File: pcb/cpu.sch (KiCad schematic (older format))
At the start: 7 parts, among them J1 Conn_01x16, J2 Conn_01x16, U1 74HC86, U2 74AHC1G08, U3 74HC86, U4 74AHC1G08, U5 74AHC1G32

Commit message: wip schematics
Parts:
- removed J1: Conn_01x16, symbol Connector_Generic:Conn_01x16
- removed U2: 74AHC1G08, symbol 74xGxx:74AHC1G08
- removed U5: 74AHC1G32, symbol 74xGxx:74AHC1G32
- added J1: Conn_01x32_Male, symbol Connector:Conn_01x32_Male
- added U10, U11, U6, U7, U8, U9: 74AHC1G08, symbol 74xGxx:74AHC1G08
- added U12, U13, U14, U2, U5: 74HC86, symbol 74xx:74HC86
- added U15, U16, U17: 74AHC1G32, symbol 74xGxx:74AHC1G32
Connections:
- wire segments 28 -> 90

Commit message: labels
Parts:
- removed J1: Conn_01x32_Male, symbol Connector:Conn_01x32_Male
- removed J2: Conn_01x16, symbol Connector_Generic:Conn_01x16
- removed U1: 74HC86, symbol 74xx:74HC86
- removed U7: 74AHC1G08, symbol 74xGxx:74AHC1G08
- added U?: 74AHC1G08, symbol 74xGxx:74AHC1G08
- added U?: 74HC86, symbol 74xx:74HC86
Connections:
- net labels added: a0, a1, a2, a3, b0, b1, b2, b3, sum0, sum1, sum2, sum3
- wire segments 90 -> 74
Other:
- moved on the sheet: U10, U11, U12A, U13A, U14A, U15, U16, U17, U2A, U3A, U4, U5A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

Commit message: 16bit adder
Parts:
- added U1, U21, U23, U24, U25, U26, U35, U36, U37, U38, U43, U44, U45, U46, U55, U56, U57, U58, U63, U64, U65, U72, U73, U74: 74HC86, symbol 74xx:74HC86
- added U19, U20, U27, U28, U29, U30, U31, U32, U33, U34, U47, U48, U49, U50, U51, U52, U53, U54, U66, U67, U68, U69, U70, U71: 74AHC1G08, symbol 74xGxx:74AHC1G08
- added U22, U39, U40, U41, U42, U59, U60, U61, U62, U75, U76, U77: 74AHC1G32, symbol 74xGxx:74AHC1G32
- gave numbers to parts that had none: 2
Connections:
- net GND: now also U19.3 (GND), U20.3 (GND), U22.3 (GND), U27.3 (GND), U28.3 (GND), U29.3 (GND), U30.3 (GND), U31.3 (GND), U32.3 (GND), U33.3 (GND), U34.3 (GND), U39.3 (GND), U40.3 (GND), U41.3 (GND), U42.3 (GND), U47.3 (GND), U48.3 (GND), U49.3 (GND), U50.3 (GND), U51.3 (GND), U52.3 (GND), U53.3 (GND), U54.3 (GND), U59.3 (GND), U60.3 (GND), U61.3 (GND), U62.3 (GND), U66.3 (GND), U67.3 (GND), U68.3 (GND), U69.3 (GND), U70.3 (GND), U71.3 (GND), U75.3 (GND), U76.3 (GND), U77.3 (GND)
- net VCC: now also U19.5 (VCC), U20.5 (VCC), U22.5 (VCC), U27.5 (VCC), U28.5 (VCC), U29.5 (VCC), U30.5 (VCC), U31.5 (VCC), U32.5 (VCC), U33.5 (VCC), U34.5 (VCC), U39.5 (VCC), U40.5 (VCC), U41.5 (VCC), U42.5 (VCC), U47.5 (VCC), U48.5 (VCC), U49.5 (VCC), U50.5 (VCC), U51.5 (VCC), U52.5 (VCC), U53.5 (VCC), U54.5 (VCC), U59.5 (VCC), U60.5 (VCC), U61.5 (VCC), U62.5 (VCC), U66.5 (VCC), U67.5 (VCC), U68.5 (VCC), U69.5 (VCC), U70.5 (VCC), U71.5 (VCC), U75.5 (VCC), U76.5 (VCC), U77.5 (VCC)
- net at U16.4: now also U19.1, U21.1
- new net: U19.4, U22.1
- new net: U20.4, U22.2
- new net: U22.4, U27.1, U35.1
- new net: U1.3, U19.2, U21.2
- new net: U27.4, U39.1
- new net: U28.4, U39.2
- new net: U29.1, U36.1, U39.4
- new net: U23.3, U27.2, U35.2
- new net: U29.4, U40.1
- new net: U30.4, U40.2
- new net: U31.1, U37.1, U40.4
- new net: U24.3, U29.2, U36.2
- new net: U31.4, U41.1
- new net: U32.4, U41.2
- new net: U33.1, U38.1, U41.4
- new net: U25.3, U31.2, U37.2
- new net: U33.4, U42.1
- new net: U34.4, U42.2
- new net: U42.4, U47.1, U55.1
- new net: U26.3, U33.2, U38.2
- new net: U47.4, U59.1
- new net: U48.4, U59.2
- new net: U49.1, U56.1, U59.4
- new net: U43.3, U47.2, U55.2
- new net: U49.4, U60.1
- new net: U50.4, U60.2
- new net: U51.1, U57.1, U60.4
- new net: U44.3, U49.2, U56.2
- new net: U51.4, U61.1
- new net: U52.4, U61.2
- new net: U53.1, U58.1, U61.4
- new net: U45.3, U51.2, U57.2
- new net: U53.4, U62.1
- new net: U54.4, U62.2
- new net: U62.4, U66.1, U72.1
- new net: U46.3, U53.2, U58.2
- new net: U66.4, U75.1
- new net: U67.4, U75.2
- new net: U68.1, U73.1, U75.4
- new net: U63.3, U66.2, U72.2
- new net: U68.4, U76.1
- new net: U69.4, U76.2
- new net: U70.1, U74.1, U76.4
- new net: U64.3, U68.2, U73.2
- new net: U70.4, U77.1
- new net: U71.4, U77.2
- new net: U65.3, U70.2, U74.2
- new net a10: U44.1, U50.1
- new net a11: U45.1, U52.1
- new net a12: U46.1, U54.1
- new net a13: U63.1, U67.1
- new net a14: U64.1, U69.1
- new net a15: U65.1, U71.1
- new net a4: U1.1, U20.1
- new net a5: U23.1, U28.1
- new net a6: U24.1, U30.1
- new net a7: U25.1, U32.1
- new net a8: U26.1, U34.1
- new net a9: U43.1, U48.1
- new net b10: U44.2, U50.2
- new net b11: U45.2, U52.2
- new net b12: U46.2, U54.2
- new net b13: U63.2, U67.2
- new net b14: U64.2, U69.2
- new net b15: U65.2, U71.2
- new net b4: U1.2, U20.2
- new net b5: U23.2, U28.2
- new net b6: U24.2, U30.2
- new net b7: U25.2, U32.2
- new net b8: U26.2, U34.2
- new net b9: U43.2, U48.2
- new net c: U77.4
- new net sum10: U56.3
- new net sum11: U57.3
- new net sum12: U58.3
- new net sum13: U72.3
- new net sum14: U73.3
- new net sum15: U74.3
- new net sum4: U21.3
- new net sum5: U35.3
- new net sum6: U36.3
- new net sum7: U37.3
- new net sum8: U38.3
- new net sum9: U55.3
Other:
- moved on the sheet: U10, U11, U12A, U13A, U14A, U15, U16, U17, U18, U2A, U3A, U4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

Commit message: adder 16 bit netlist and footprints
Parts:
- U1, U10, U11, U12, U13, U14, U15, U16, U17, U18, U19, U2, U20, U21, U22, U23, U24, U25, U26, U27, U28, U29, U3, U30, U31, U32, U33, U34, U35, U36, U37, U38, U39, U4, U40, U41, U42, U43, U44, U45, U46, U47, U48, U49, U5, U50, U51, U52, U53, U54, U55, U56, U57, U58, U59, U6, U60, U61, U62, U63, U64, U65, U66, U67, U68, U69, U7, U70, U71, U72, U73, U74, U75, U76, U77, U8, U9: footprint (none) -> Package_SO:SOIC-14_3.9x8.7mm_P1.27mm

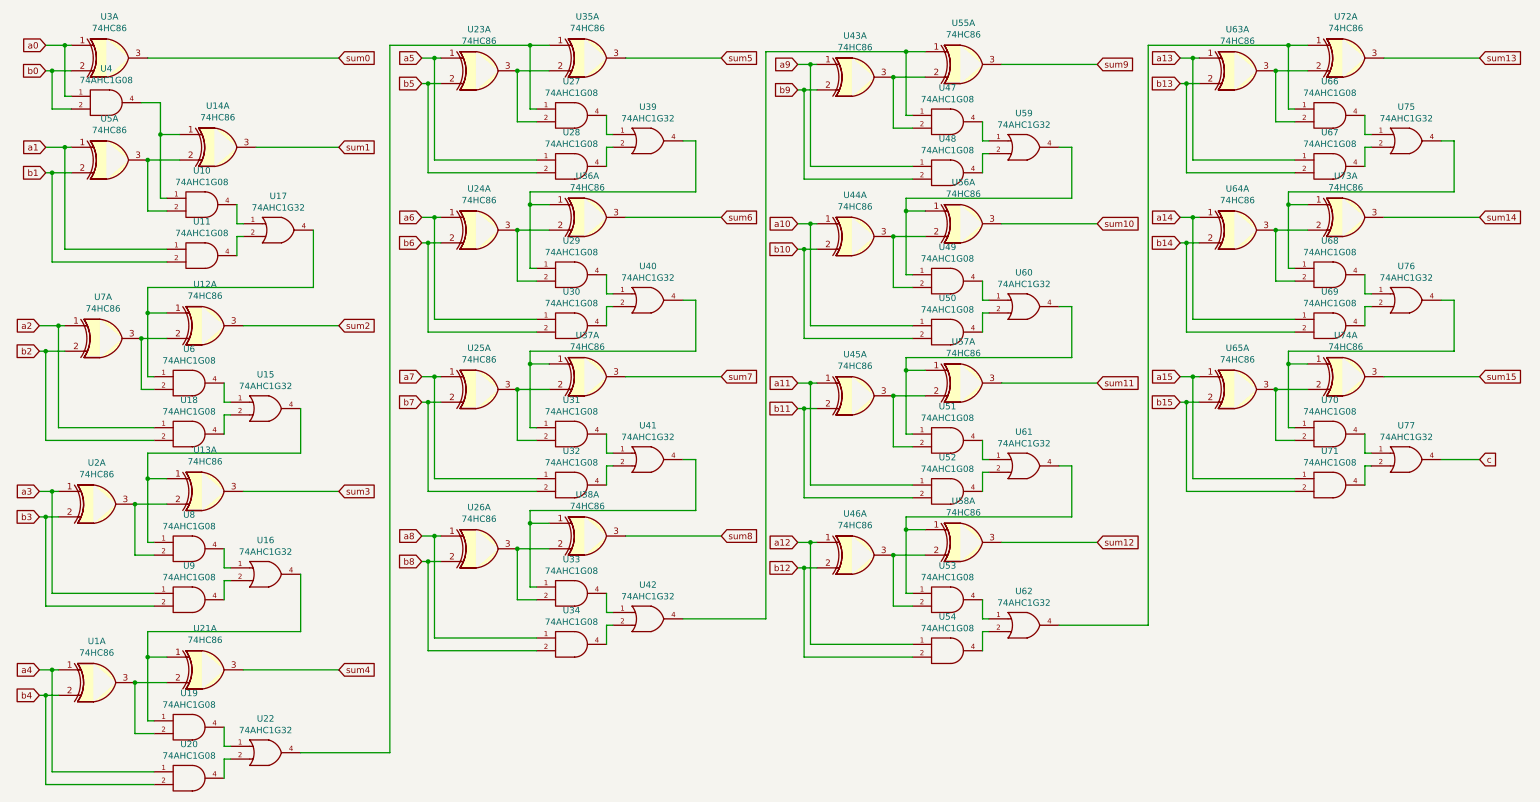
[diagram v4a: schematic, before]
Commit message: 16 bit adder from 74LS283
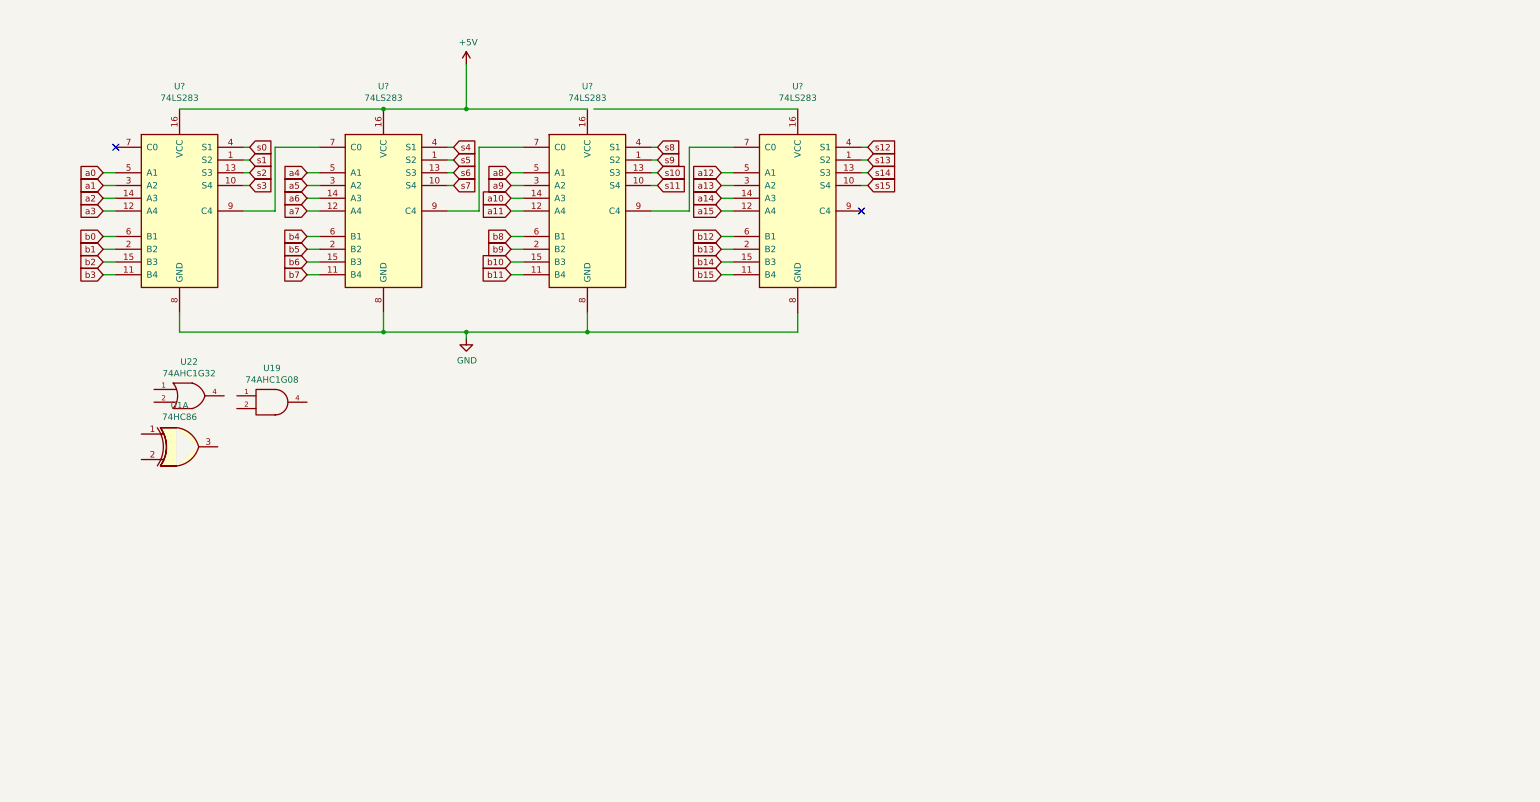
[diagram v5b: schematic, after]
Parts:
- removed U10, U11, U18, U20, U27, U28, U29, U30, U31, U32, U33, U34, U4, U47, U48, U49, U50, U51, U52, U53, U54, U6, U66, U67, U68, U69, U70, U71, U8, U9: 74AHC1G08, Package_SO:SOIC-14_3.9x8.7mm_P1.27mm, symbol 74xGxx:74AHC1G08
- removed U12, U13, U14, U2, U21, U23, U24, U25, U26, U3, U35, U36, U37, U38, U43, U44, U45, U46, U5, U55, U56, U57, U58, U63, U64, U65, U7, U72, U73, U74: 74HC86, Package_SO:SOIC-14_3.9x8.7mm_P1.27mm, symbol 74xx:74HC86
- removed U15, U16, U17, U39, U40, U41, U42, U59, U60, U61, U62, U75, U76, U77: 74AHC1G32, Package_SO:SOIC-14_3.9x8.7mm_P1.27mm, symbol 74xGxx:74AHC1G32
- added U? (x4): 74LS283, symbol 74xx:74LS283
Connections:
- net GND: now also U?.8 (GND), U?.8 (GND), U?.8 (GND), U?.8 (GND)
- net a0: now also U?.5 (A1)
- net a1: now also U?.3 (A2)
- net a10: now also U?.14 (A3)
- net a11: now also U?.12 (A4)
- net a12: now also U?.5 (A1)
- net a13: now also U?.3 (A2)
- net a14: now also U?.14 (A3)
- net a15: now also U?.12 (A4)
- net a2: now also U?.14 (A3)
- net a3: now also U?.12 (A4)
- net a4: now also U?.5 (A1); no longer U1.1
- net a5: now also U?.3 (A2)
- net a6: now also U?.14 (A3)
- net a7: now also U?.12 (A4)
- net a8: now also U?.5 (A1)
- net a9: now also U?.3 (A2)
- net b0: now also U?.6 (B1)
- net b1: now also U?.2 (B2)
- net b10: now also U?.15 (B3)
- net b11: now also U?.11 (B4)
- net b12: now also U?.6 (B1)
- net b13: now also U?.2 (B2)
- net b14: now also U?.15 (B3)
- net b15: now also U?.11 (B4)
- net b2: now also U?.15 (B3)
- net b3: now also U?.11 (B4)
- net b4: now also U?.6 (B1); no longer U1.2
- net b5: now also U?.2 (B2)
- net b6: now also U?.15 (B3)
- net b7: now also U?.11 (B4)
- net b8: now also U?.6 (B1)
- net b9: now also U?.2 (B2)
- net at U22.1: no longer U19.4
- net at U19.2: no longer U1.3
- new net: U?.7 (C0), U?.9 (C4) (x3)
- new net +5V: U?.16 (VCC), U?.16 (VCC), U?.16 (VCC)
- new net s0: U?.4 (S1)
- new net s1: U?.1 (S2)
- new net s10: U?.13 (S3)
- new net s11: U?.10 (S4)
- new net s12: U?.4 (S1)
- new net s13: U?.1 (S2)
- new net s14: U?.13 (S3)
- new net s15: U?.10 (S4)
- new net s2: U?.13 (S3)
- new net s3: U?.10 (S4)
- new net s4: U?.4 (S1)
- new net s5: U?.1 (S2)
- new net s6: U?.13 (S3)
- new net s7: U?.10 (S4)
- new net s8: U?.4 (S1)
- new net s9: U?.1 (S2)
- no-connect marks 0 -> 2
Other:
- moved on the sheet: U19, U1A, U22

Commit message: wip
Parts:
- removed U1: 74HC86, Package_SO:SOIC-14_3.9x8.7mm_P1.27mm, symbol 74xx:74HC86
- removed U19: 74AHC1G08, Package_SO:SOIC-14_3.9x8.7mm_P1.27mm, symbol 74xGxx:74AHC1G08
- removed U22: 74AHC1G32, Package_SO:SOIC-14_3.9x8.7mm_P1.27mm, symbol 74xGxx:74AHC1G32
- added J1: Conn_02x16_Counter_Clockwise, Connector_PinHeader_1.27mm:PinHeader_2x16_P1.27mm_Vertical, symbol Connector_Generic:Conn_02x16_Counter_Clockwise
- added J2: Conn_01x16, Connector_PinHeader_1.27mm:PinHeader_1x16_P1.27mm_Vertical, symbol Connector_Generic:Conn_01x16
- added U? (x3): 74LS21, symbol 74xx:74LS21
- U1, U2, U3, U4: renamed from U?; footprint (none) -> Package_SO:SOIC-16_3.9x9.9mm_P1.27mm
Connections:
- net a0: now also J1.1 (Pin_1)
- net a1: now also J1.2 (Pin_2)
- net a10: now also J1.11 (Pin_11)
- net a11: now also J1.12 (Pin_12)
- net a12: now also J1.13 (Pin_13)
- net a13: now also J1.14 (Pin_14)
- net a14: now also J1.15 (Pin_15)
- net a15: now also J1.16 (Pin_16)
- net a2: now also J1.3 (Pin_3)
- net a3: now also J1.4 (Pin_4)
- net a4: now also J1.5 (Pin_5)
- net a5: now also J1.6 (Pin_6)
- net a6: now also J1.7 (Pin_7)
- net a7: now also J1.8 (Pin_8)
- net a8: now also J1.9 (Pin_9)
- net a9: now also J1.10 (Pin_10)
- net b0: now also J1.32 (Pin_32)
- net b1: now also J1.31 (Pin_31)
- net b10: now also J1.22 (Pin_22)
- net b11: now also J1.21 (Pin_21)
- net b12: now also J1.20 (Pin_20)
- net b13: now also J1.19 (Pin_19)
- net b14: now also J1.18 (Pin_18)
- net b15: now also J1.17 (Pin_17)
- net b2: now also J1.30 (Pin_30)
- net b3: now also J1.29 (Pin_29)
- net b4: now also J1.28 (Pin_28)
- net b5: now also J1.27 (Pin_27)
- net b6: now also J1.26 (Pin_26)
- net b7: now also J1.25 (Pin_25)
- net b8: now also J1.24 (Pin_24)
- net b9: now also J1.23 (Pin_23)
- net s0: now also J2.1 (Pin_1)
- net s1: now also J2.2 (Pin_2)
- net s10: now also J2.11 (Pin_11)
- net s11: now also J2.12 (Pin_12)
- net s12: now also J2.13 (Pin_13)
- net s13: now also J2.14 (Pin_14)
- net s14: now also J2.15 (Pin_15)
- net s15: now also J2.16 (Pin_16)
- net s2: now also J2.3 (Pin_3)
- net s3: now also J2.4 (Pin_4)
- net s4: now also J2.5 (Pin_5)
- net s5: now also J2.6 (Pin_6)
- net s6: now also J2.7 (Pin_7)
- net s7: now also J2.8 (Pin_8)
- net s8: now also J2.9 (Pin_9)
- net s9: now also J2.10 (Pin_10)
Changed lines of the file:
@@
 $EndDescr
 $Comp
-L 74xx:74LS283 U?
+L 74xx:74LS283 U1
 U 1 1 5CE54893
 P 1750 2100
-F 0 "U?" H 1750 3078 50  0000 C CNN
+F 0 "U1" H 1750 3078 50  0000 C CNN
 F 1 "74LS283" H 1750 2987 50  0000 C CNN
-F 2 "" H 1750 2100 50  0001 C CNN
+F 2 "Package_SO:SOIC-16_3.9x9.9mm_P1.27mm" H 1750 2100 50  0001 C CNN
 F 3 "http://www.ti.com/lit/gpn/sn74LS283" H 1750 2100 50  0001 C CNN
 	1    1750 2100
@@
 $EndComp
 $Comp
-L 74xx:74LS283 U?
+L 74xx:74LS283 U2
 U 1 1 5CE54F63
 P 3350 2100
-F 0 "U?" H 3350 3078 50  0000 C CNN
+F 0 "U2" H 3350 3078 50  0000 C CNN
 F 1 "74LS283" H 3350 2987 50  0000 C CNN
-F 2 "" H 3350 2100 50  0001 C CNN
+F 2 "Package_SO:SOIC-16_3.9x9.9mm_P1.27mm" H 3350 2100 50  0001 C CNN
 F 3 "http://www.ti.com/lit/gpn/sn74LS283" H 3350 2100 50  0001 C CNN
 	1    3350 2100
@@
 $EndComp
 $Comp
-L 74xx:74HC86 U1
-U 1 1 5CC11E00
-P 1750 3950
-F 0 "U1" H 1750 4275 50  0000 C CNN
-F 1 "74HC86" H 1750 4184 50  0000 C CNN
-F 2 "Package_SO:SOIC-14_3.9x8.7mm_P1.27mm" H 1750 3950 50  0001 C CNN
-F 3 "http://www.ti.com/lit/gpn/sn74HC86" H 1750 3950 50  0001 C CNN
-	1    1750 3950
-	1    0    0    -1
-$EndComp
-$Comp
-L 74xGxx:74AHC1G08 U19
-U 1 1 5CC11DE5
-P 2500 3600
-F 0 "U19" H 2475 3867 50  0000 C CNN
-F 1 "74AHC1G08" H 2475 3776 50  0000 C CNN
-F 2 "Package_SO:SOIC-14_3.9x8.7mm_P1.27mm" H 2500 3600 50  0001 C CNN
-F 3 "http://www.ti.com/lit/sg/scyt129e/scyt129e.pdf" H 2500 3600 50  0001 C CNN
-	1    2500 3600
-	1    0    0    -1
-$EndComp
-$Comp
-L 74xGxx:74AHC1G32 U22
-U 1 1 5CC11DD7
-P 1850 3550
-F 0 "U22" H 1825 3817 50  0000 C CNN
-F 1 "74AHC1G32" H 1825 3726 50  0000 C CNN
-F 2 "Package_SO:SOIC-14_3.9x8.7mm_P1.27mm" H 1850 3550 50  0001 C CNN
-F 3 "http://www.ti.com/lit/sg/scyt129e/scyt129e.pdf" H 1850 3550 50  0001 C CNN
-	1    1850 3550
-	1    0    0    -1
-$EndComp
-$Comp
-L power:+5V #PWR?
+L power:+5V #PWR0101
 U 1 1 5CE5585C
 P 4000 950
-F 0 "#PWR?" H 4000 800 50  0001 C CNN
+F 0 "#PWR0101" H 4000 800 50  0001 C CNN
 F 1 "+5V" H 4015 1123 50  0000 C CNN
 F 2 "" H 4000 950 50  0001 C CNN
@@
 $EndComp
 $Comp
-L 74xx:74LS283 U?
+L 74xx:74LS283 U3
 U 1 1 5CE55A6B
 P 4950 2100
-F 0 "U?" H 4950 3078 50  0000 C CNN
+F 0 "U3" H 4950 3078 50  0000 C CNN
 F 1 "74LS283" H 4950 2987 50  0000 C CNN
-F 2 "" H 4950 2100 50  0001 C CNN
+F 2 "Package_SO:SOIC-16_3.9x9.9mm_P1.27mm" H 4950 2100 50  0001 C CNN
 F 3 "http://www.ti.com/lit/gpn/sn74LS283" H 4950 2100 50  0001 C CNN
 	1    4950 2100
@@
 $EndComp
 $Comp
-L 74xx:74LS283 U?
+L 74xx:74LS283 U4
 U 1 1 5CE55A72
 P 6600 2100
-F 0 "U?" H 6600 3078 50  0000 C CNN
+F 0 "U4" H 6600 3078 50  0000 C CNN
 F 1 "74LS283" H 6600 2987 50  0000 C CNN
-F 2 "" H 6600 2100 50  0001 C CNN
+F 2 "Package_SO:SOIC-16_3.9x9.9mm_P1.27mm" H 6600 2100 50  0001 C CNN
 F 3 "http://www.ti.com/lit/gpn/sn74LS283" H 6600 2100 50  0001 C CNN
 	1    6600 2100
@@
 	1750 3050 1750 2900
 $Comp
-L power:GND #PWR?
+L power:GND #PWR0102
 U 1 1 5CE55F14
 P 4000 3100
-F 0 "#PWR?" H 4000 2850 50  0001 C CNN
+F 0 "#PWR0102" H 4000 2850 50  0001 C CNN
 F 1 "GND" H 4005 2927 50  0000 C CNN
 F 2 "" H 4000 3100 50  0001 C CNN
@@
 	4950 3050 6600 3050
 Connection ~ 4950 3050
+$Comp
+L Connector_Generic:Conn_02x16_Counter_Clockwise J1
+U 1 1 5CAD3D15
+P 1550 4300
+F 0 "J1" H 1600 5217 50  0000 C CNN
+F 1 "Conn_02x16_Counter_Clockwise" H 1600 5126 50  0000 C CNN
+F 2 "Connector_PinHeader_1.27mm:PinHeader_2x16_P1.27mm_Vertical" H 1550 4300 50  0001 C CNN
+F 3 "~" H 1550 4300 50  0001 C CNN
+	1    1550 4300
+	1    0    0    -1
+$EndComp
+Text GLabel 1350 3600 0    50   Input ~ 0
+a0
+Text GLabel 1350 3700 0    50   Input ~ 0
+a1
+Text GLabel 1350 3800 0    50   Input ~ 0
+a2
+Text GLabel 1350 3900 0    50   Input ~ 0
+a3
+Text GLabel 1350 4000 0    50   Input ~ 0
+a4
+Text GLabel 1350 4100 0    50   Input ~ 0
+a5
+Text GLabel 1350 4200 0    50   Input ~ 0
+a6
+Text GLabel 1350 4300 0    50   Input ~ 0
+a7
+Text GLabel 1350 4400 0    50   Input ~ 0
+a8
+Text GLabel 1350 4500 0    50   Input ~ 0
+a9
+Text GLabel 1350 4600 0    50   Input ~ 0
+a10
+Text GLabel 1350 4700 0    50   Input ~ 0
+a11
+Text GLabel 1350 4800 0    50   Input ~ 0
+a12
+Text GLabel 1350 4900 0    50   Input ~ 0
+a13
+Text GLabel 1350 5000 0    50   Input ~ 0
+a14
+Text GLabel 1350 5100 0    50   Input ~ 0
+a15
+Text GLabel 1850 3600 2    50   Input ~ 0
+b0
+Text GLabel 1850 3700 2    50   Input ~ 0
+b1
+Text GLabel 1850 3800 2    50   Input ~ 0
+b2
+Text GLabel 1850 3900 2    50   Input ~ 0
+b3
+Text GLabel 1850 4000 2    50   Input ~ 0
+b4
+Text GLabel 1850 4100 2    50   Input ~ 0
+b5
+Text GLabel 1850 4200 2    50   Input ~ 0
+b6
+Text GLabel 1850 4300 2    50   Input ~ 0
+b7
+Text GLabel 1850 4400 2    50   Input ~ 0
+b8
+Text GLabel 1850 4500 2    50   Input ~ 0
+b9
+Text GLabel 1850 4600 2    50   Input ~ 0
+b10
+Text GLabel 1850 4700 2    50   Input ~ 0
+b11
+Text GLabel 1850 4800 2    50   Input ~ 0
+b12
+Text GLabel 1850 4900 2    50   Input ~ 0
+b13
+Text GLabel 1850 5000 2    50   Input ~ 0
+b14
+Text GLabel 1850 5100 2    50   Input ~ 0
+b15
+$Comp
+L Connector_Generic:Conn_01x16 J2
+U 1 1 5CADB34A
+P 2850 4300
+F 0 "J2" H 2930 4292 50  0000 L CNN
+F 1 "Conn_01x16" H 2930 4201 50  0000 L CNN
+F 2 "Connector_PinHeader_1.27mm:PinHeader_1x16_P1.27mm_Vertical" H 2850 4300 50  0001 C CNN
+F 3 "~" H 2850 4300 50  0001 C CNN
+	1    2850 4300
+	1    0    0    -1
+$EndComp
+Text GLabel 2650 3600 0    50   Input ~ 0
+s0
+Text GLabel 2650 3700 0    50   Input ~ 0
+s1
+Text GLabel 2650 3800 0    50   Input ~ 0
+s2
+Text GLabel 2650 3900 0    50   Input ~ 0
+s3
+Text GLabel 2650 4000 0    50   Input ~ 0
+s4
+Text GLabel 2650 4100 0    50   Input ~ 0
+s5
+Text GLabel 2650 4200 0    50   Input ~ 0
+s6
+Text GLabel 2650 4300 0    50   Input ~ 0
+s7
+Text GLabel 2650 4400 0    50   Input ~ 0
+s8
+Text GLabel 2650 4500 0    50   Input ~ 0
+s9
+Text GLabel 2650 4600 0    50   Input ~ 0
+s10
+Text GLabel 2650 4700 0    50   Input ~ 0
+s11
+Text GLabel 2650 4800 0    50   Input ~ 0
+s12
+Text GLabel 2650 4900 0    50   Input ~ 0
+s13
+Text GLabel 2650 5000 0    50   Input ~ 0
+s14
+Text GLabel 2650 5100 0    50   Input ~ 0
+s15
+$Comp
+L 74xx:74LS21 U?
+U 1 1 5CAE1172
+P 4900 4000
+F 0 "U?" H 4900 4375 50  0000 C CNN
+F 1 "74LS21" H 4900 4284 50  0000 C CNN
+F 2 "" H 4900 4000 50  0001 C CNN
+F 3 "http://www.ti.com/lit/gpn/sn74LS21" H 4900 4000 50  0001 C CNN
+	1    4900 4000
+	1    0    0    -1
+$EndComp
+$Comp
+L 74xx:74LS21 U?
+U 1 1 5CAE121A
+P 4900 4600
+F 0 "U?" H 4900 4975 50  0000 C CNN
+F 1 "74LS21" H 4900 4884 50  0000 C CNN
+F 2 "" H 4900 4600 50  0001 C CNN
+F 3 "http://www.ti.com/lit/gpn/sn74LS21" H 4900 4600 50  0001 C CNN
+	1    4900 4600
+	1    0    0    -1
+$EndComp
+$Comp
+L 74xx:74LS21 U?
+U 1 1 5CAE2EBC
+P 4900 5200
+F 0 "U?" H 4900 5575 50  0000 C CNN
+F 1 "74LS21" H 4900 5484 50  0000 C CNN
+F 2 "" H 4900 5200 50  0001 C CNN
+F 3 "http://www.ti.com/lit/gpn/sn74LS21" H 4900 5200 50  0001 C CNN
+	1    4900 5200
+	1    0    0    -1
+$EndComp
 $EndSCHEMATC
